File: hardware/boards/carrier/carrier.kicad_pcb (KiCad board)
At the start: 4 copper layers, 106 x 34.3 mm, 64 parts, among them J1 XT30PW(2+2), Q1 IPB020N10N5LF, Q2 2N7002, Q3 2N7002, SW1 SKSCLCE010, U1 STM32C092GCU7, U2 LM5163DDAR, U3 LMX5069MS, U4 INA237AIDGSR, U5 TCAN3413DR

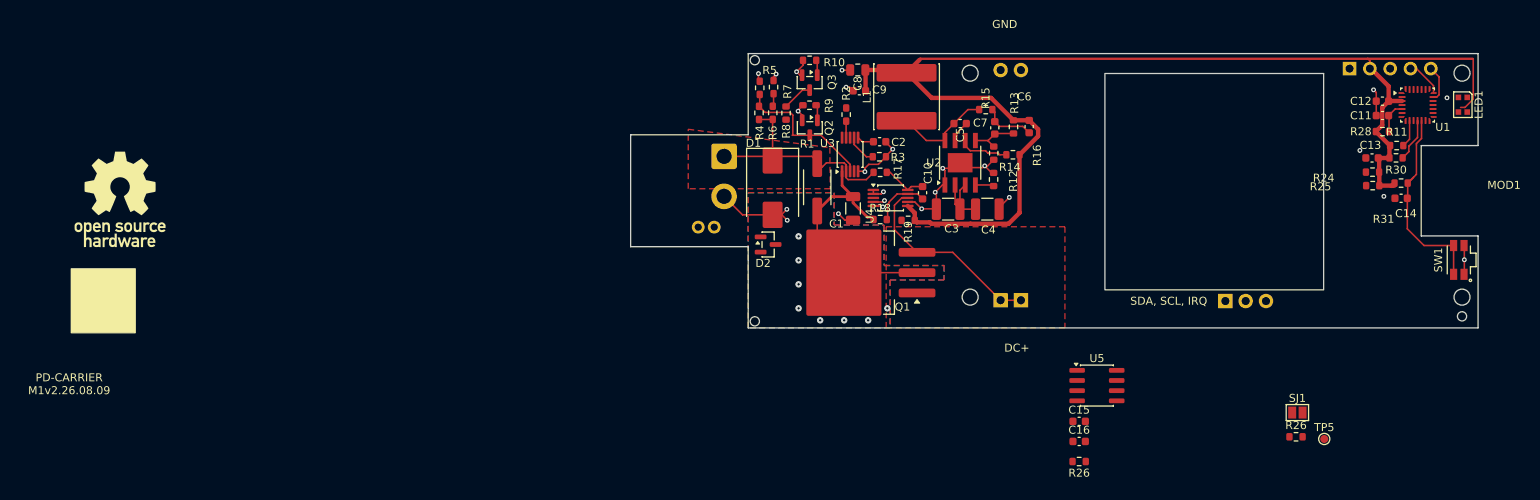
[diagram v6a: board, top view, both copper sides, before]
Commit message: Refine carrier PCB placement
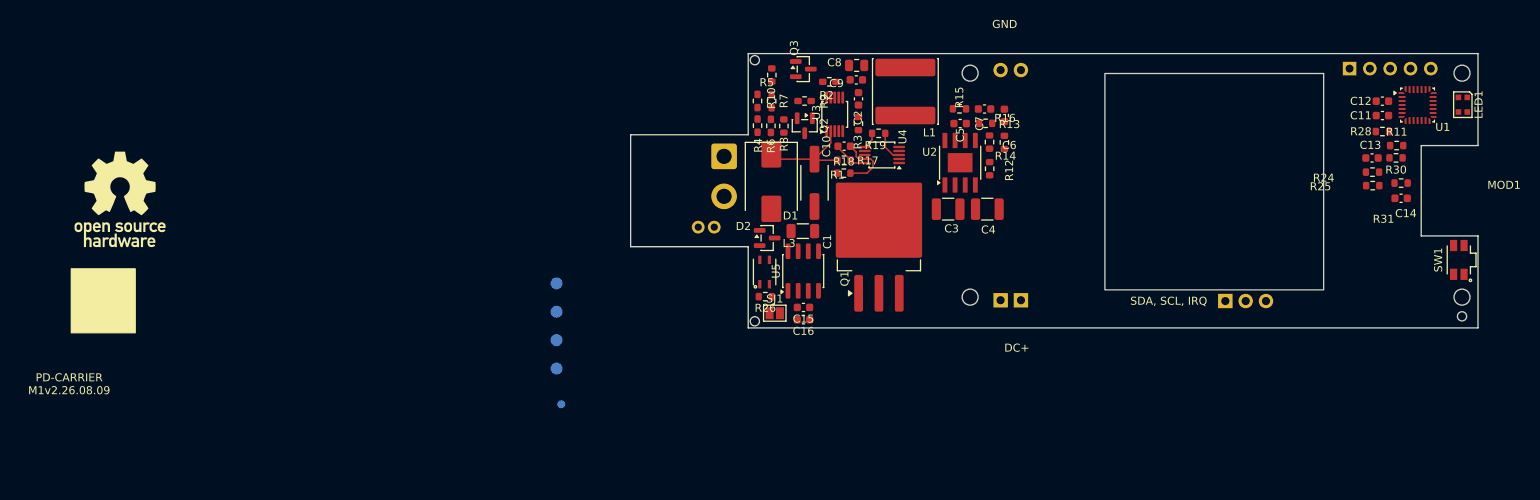
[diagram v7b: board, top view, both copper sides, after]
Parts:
- removed the R26 at (184.0, 144.3)
- added L3: ACT1210D-101-2P-TL00, mini-rack-power:L_CommonModeChoke_TDK_ACT1210D, F.Cu at (117.5, 123.7)
- added TP17: CANH_BUS, TestPoint:TestPoint_Pad_D1.5mm, B.Cu at (91.5, 132.2)
- added TP18: CANL_BUS, TestPoint:TestPoint_Pad_D1.5mm, B.Cu at (91.5, 135.7)
- added TP6: CAN_RX, TestPoint:TestPoint_Pad_D1.5mm, B.Cu at (91.5, 125.1)
- added TP7: CAN_TX, TestPoint:TestPoint_Pad_D1.5mm, B.Cu at (91.5, 128.6)
- TP5: moved to B.Cu
- moved TP5 95.5 mm to (92.1, 140.2), turned to 180 degrees
- moved SJ1 66.5 mm to (118.8, 128.8)
- moved R26 44.3 mm to (117.6, 126.7)
- moved U5 39.4 mm to (122.4, 123.5), turned to 90 degrees
- moved C16 37.7 mm to (122.4, 129.6), turned to 180 degrees
- moved C15 37.3 mm to (122.4, 128.1), turned to 180 degrees
- moved R19 11.5 mm to (131.8, 106.3), turned to 0 degrees
- moved C10 11.4 mm to (127.5, 107.9), turned to 0 degrees
- moved R18 7.37 mm to (127.5, 111.3)
- moved C1 6.89 mm to (122.3, 118.5), turned to 180 degrees
- moved C2 5.97 mm to (129.3, 102.0), turned to -90 degrees
- moved Q1 5.83 mm to (131.8, 118.7), turned to 90 degrees
- moved U4 5.48 mm to (132.2, 109.0), turned to 180 degrees
- moved U3 5.36 mm to (126.3, 104.0)
- moved R10 5.08 mm to (118.5, 99.0), turned to -90 degrees
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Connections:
- D2 pad 1: /Protected Power and Controls/CANH_BUS -> /CANH_BUS
- D2 pad 2: /Protected Power and Controls/CANL_BUS -> /CANL_BUS
- U5 pad 3: Net-(U5-VCC) -> +3V3
- U5 pad 5: Net-(U5-VCC) -> +3V3
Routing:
- net +3V3: track 157.3 -> 2.09 mm
- net GND: track 57.0 -> 0.00 mm, vias 22 -> 0
- net /Protected Power and Controls/HS_SENSE: track 31.6 -> 0.00 mm, vias 8 -> 0
- net /STM32 Housekeeping and Status/USER_BUTTON_N: track 25.6 -> 0.00 mm
- net /Protected Power and Controls/PD_VIN_SW: track 24.6 -> 0.00 mm
- net VCC: track 37.0 -> 12.9 mm
- net /Protected Power and Controls/HS_UVLO: track 18.3 -> 0.00 mm
- net /BUCK_SW: track 12.3 -> 0.00 mm
- net Net-(C6-Pad1): track 6.51 -> 0.00 mm
- net /BUCK_PGOOD: track 6.26 -> 0.00 mm
- net /BUCK_FB: track 6.17 -> 0.00 mm
- net /PD_IRQ: track 5.90 -> 0.00 mm
- net /Protected Power and Controls/KILL_GATE: track 5.74 -> 0.00 mm
- net /STM32 Housekeeping and Status/SWCLK: track 4.68 -> 0.00 mm
- net /STM32 Housekeeping and Status/SWDIO: track 4.56 -> 0.00 mm
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- removed copper zone on B.Cu, net /Protected Power and Controls/HS_SENSE
- removed copper zone on F.Cu, net /Protected Power and Controls/HS_SENSE
- removed copper zone on F.Cu, net /Protected Power and Controls/PD_VIN_SW
- removed copper zone on F.Cu, net VCC

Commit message: Move carrier PD enable to PC14
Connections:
- U1 pad 1: unconnected-(U1-PC14-Pad1) -> /PD_ENABLE
- U1 pad 7: /PD_ENABLE -> unconnected-(U1-PA1-Pad7)
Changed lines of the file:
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@@
 			(size 0.136863 0.136863)
 			(layers "F.Cu" "F.Mask" "F.Paste")
-			(net "unconnected-(U1-PC14-Pad1)")
+			(net "/PD_ENABLE")
 			(pinfunction "PC14_1")
-			(pintype "bidirectional+no_connect")
+			(pintype "bidirectional")
 			(options
 				(clearance outline)
@@
 			(size 0.136863 0.136863)
 			(layers "F.Cu" "F.Mask" "F.Paste")
-			(net "/PD_ENABLE")
+			(net "unconnected-(U1-PA1-Pad7)")
 			(pinfunction "PA1_7")
-			(pintype "bidirectional")
+			(pintype "bidirectional+no_connect")
 			(options
 				(clearance outline)
